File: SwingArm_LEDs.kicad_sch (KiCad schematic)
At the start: 56 parts, among them U1 LM7815_TO220, U2 MP2410AG-Z

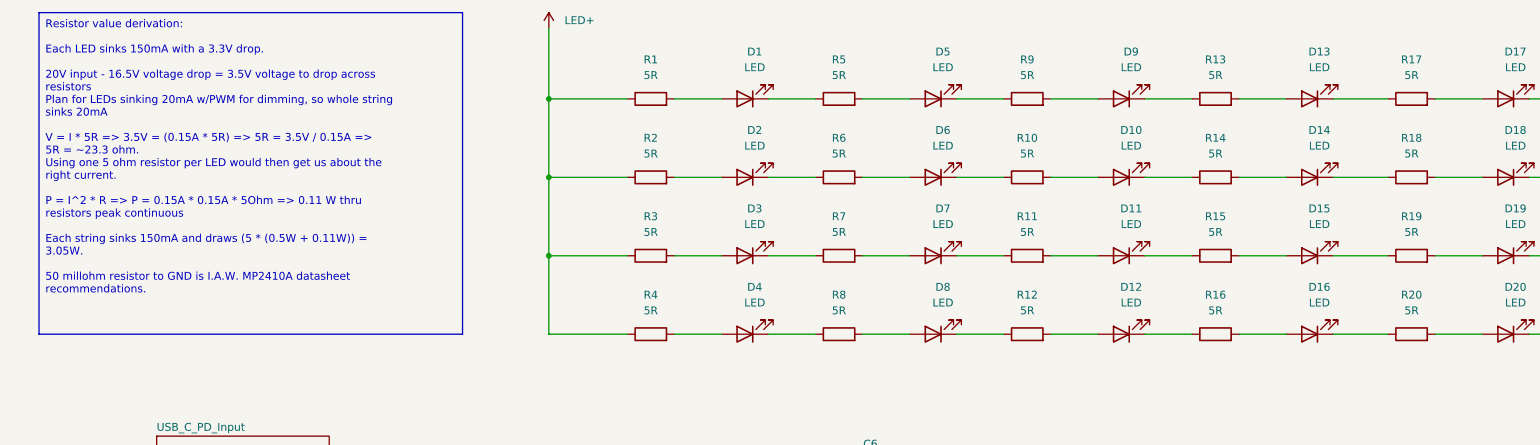
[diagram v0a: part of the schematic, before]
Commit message: Fixup resistor values
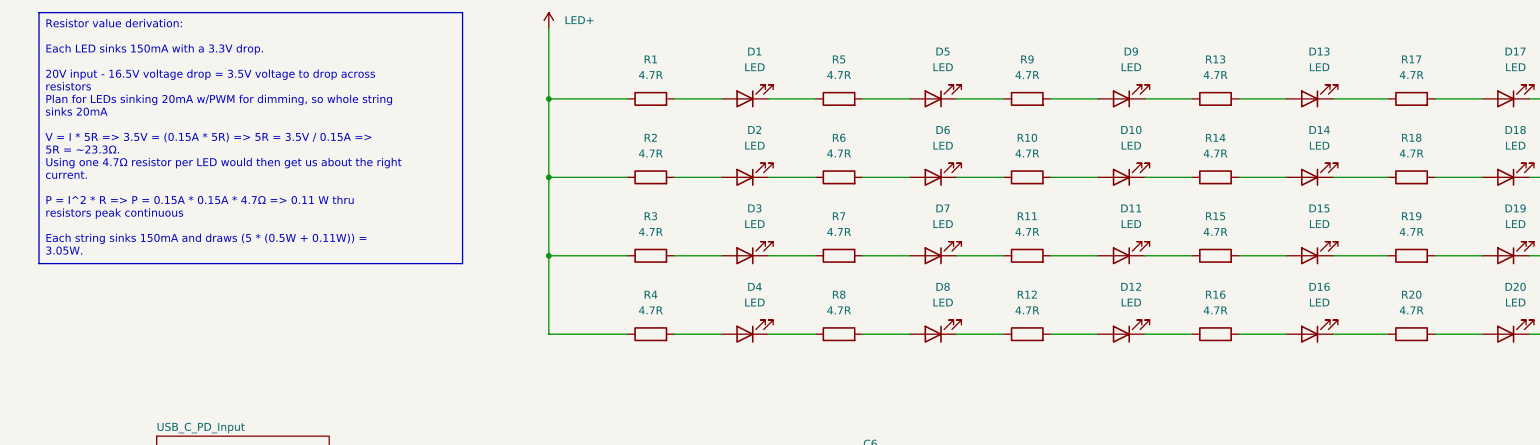
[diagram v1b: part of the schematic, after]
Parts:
- R1, R10, R11, R12, R13, R14, R15, R16, R17, R18, R19, R2, R20, R3, R4, R5, R6, R7, R8, R9: value 5R -> 4.7R
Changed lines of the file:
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@@
 		)
 	)
-	(text_box "Resistor value derivation:\n\nEach LED sinks 150mA with a 3.3V drop.\n\n20V input - 16.5V voltage drop = 3.5V voltage to drop across resistors\nPlan for LEDs sinking 20mA w/PWM for dimming, so whole string sinks 20mA\n\nV = I * 5R => 3.5V = (0.15A * 5R) => 5R = 3.5V / 0.15A => 5R = ~23.3 ohm.\nUsing one 5 ohm resistor per LED would then get us about the right current.\n\nP = I^2 * R => P = 0.15A * 0.15A * 5Ohm => 0.11 W thru resistors peak continuous\n\nEach string sinks 150mA and draws (5 * (0.5W + 0.11W)) = 3.05W.\n\n50 millohm resistor to GND is I.A.W. MP2410A datasheet recommendations."
+	(text_box "Resistor value derivation:\n\nEach LED sinks 150mA with a 3.3V drop.\n\n20V input - 16.5V voltage drop = 3.5V voltage to drop across resistors\nPlan for LEDs sinking 20mA w/PWM for dimming, so whole string sinks 20mA\n\nV = I * 5R => 3.5V = (0.15A * 5R) => 5R = 3.5V / 0.15A => 5R = ~23.3Ω.\nUsing one 4.7Ω resistor per LED would then get us about the right current.\n\nP = I^2 * R => P = 0.15A * 0.15A * 4.7Ω => 0.11 W thru resistors peak continuous\n\nEach string sinks 150mA and draws (5 * (0.5W + 0.11W)) = 3.05W."
 		(exclude_from_sim yes)
 		(at 19.05 19.05 0)
-		(size 68.58 52.07)
+		(size 68.58 40.64)
 		(stroke
 			(width 0)
@@
 			)
 		)
-		(property "Value" "5R"
+		(property "Value" "4.7R"
 			(at 148.59 41.91 90)
 			(effects
@@
 			)
 		)
-		(property "Value" "5R"
+		(property "Value" "4.7R"
 			(at 148.59 67.31 90)
 			(effects
@@
 			)
 		)
-		(property "Value" "5R"
+		(property "Value" "4.7R"
 			(at 118.11 67.31 90)
 			(effects
@@
 			)
 		)
-		(property "Value" "5R"
+		(property "Value" "4.7R"
 			(at 118.11 41.91 90)
 			(effects
@@
 			)
 		)
-		(property "Value" "5R"
+		(property "Value" "4.7R"
 			(at 179.07 41.91 90)
 			(effects
@@
 			)
 		)
-		(property "Value" "5R"
+		(property "Value" "4.7R"
 			(at 241.3 29.21 90)
 			(effects
@@
 			)
 		)
-		(property "Value" "5R"
+		(property "Value" "4.7R"
 			(at 241.3 67.31 90)
 			(effects
@@
 			)
 		)
-		(property "Value" "5R"
+		(property "Value" "4.7R"
 			(at 209.55 41.91 90)
 			(effects
@@
 			)
 		)
-		(property "Value" "5R"
+		(property "Value" "4.7R"
 			(at 241.3 54.61 90)
 			(effects
@@
 			)
 		)
-		(property "Value" "5R"
+		(property "Value" "4.7R"
 			(at 209.55 29.21 90)
 			(effects
@@
 			)
 		)
-		(property "Value" "5R"
+		(property "Value" "4.7R"
 			(at 118.11 29.21 90)
 			(effects
@@
 			)
 		)
-		(property "Value" "5R"
+		(property "Value" "4.7R"
 			(at 179.07 67.31 90)
 			(effects
@@
 			)
 		)
-		(property "Value" "5R"
+		(property "Value" "4.7R"
 			(at 179.07 54.61 90)
 			(effects
@@
 			)
 		)
-		(property "Value" "5R"
+		(property "Value" "4.7R"
 			(at 209.55 67.31 90)
 			(effects
@@
 			)
 		)
-		(property "Value" "5R"
+		(property "Value" "4.7R"
 			(at 209.55 54.61 90)
 			(effects
@@
 			)
 		)
-		(property "Value" "5R"
+		(property "Value" "4.7R"
 			(at 148.59 29.21 90)
 			(effects
@@
 			)
 		)
-		(property "Value" "5R"
+		(property "Value" "4.7R"
 			(at 179.07 29.21 90)
 			(effects
@@
 			)
 		)
-		(property "Value" "5R"
+		(property "Value" "4.7R"
 			(at 241.3 41.91 90)
 			(effects
@@
 			)
 		)
-		(property "Value" "5R"
+		(property "Value" "4.7R"
 			(at 148.59 54.61 90)
 			(effects
@@
 			)
 		)
-		(property "Value" "5R"
+		(property "Value" "4.7R"
 			(at 118.11 54.61 90)
 			(effects

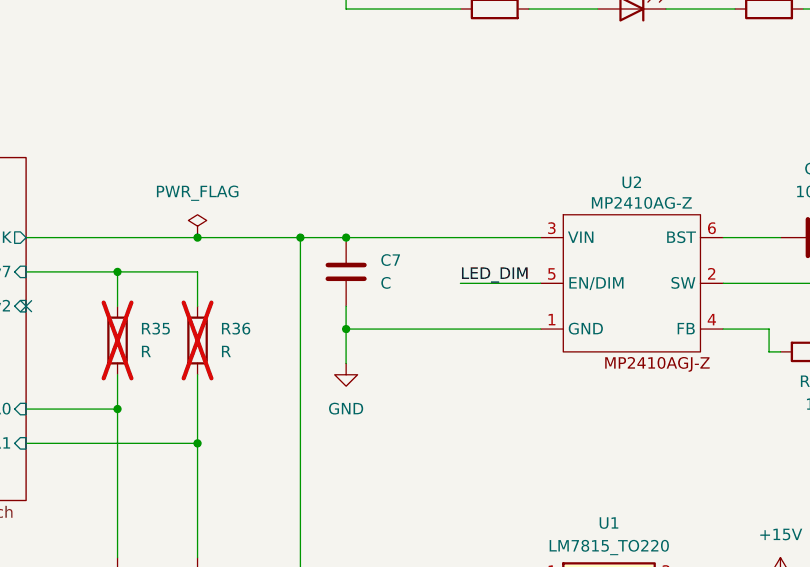
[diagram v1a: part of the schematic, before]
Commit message: Fix capacitor value
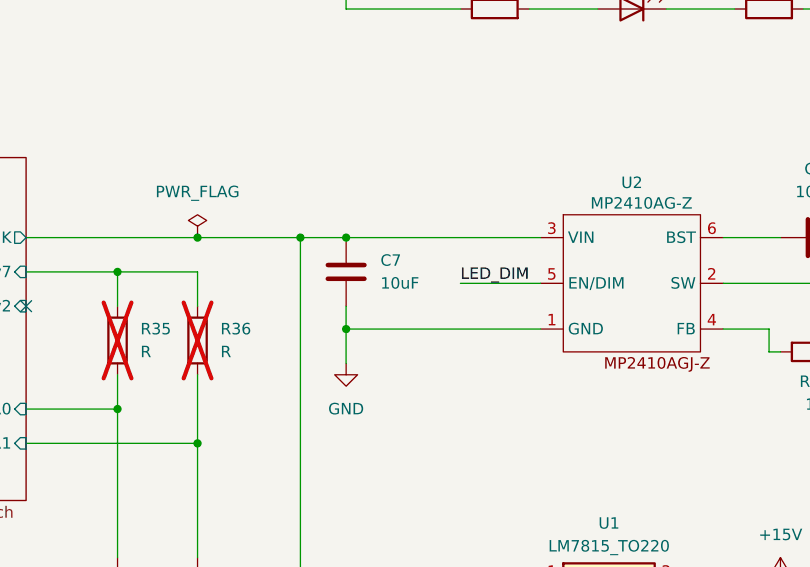
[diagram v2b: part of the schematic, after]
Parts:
- C7: value C -> 10uF
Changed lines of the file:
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@@
 			)
 		)
-		(property "Value" "C"
+		(property "Value" "10uF"
 			(at 105.41 101.5999 0)
 			(effects
